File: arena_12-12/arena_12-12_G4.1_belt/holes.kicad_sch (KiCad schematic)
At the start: 4 parts

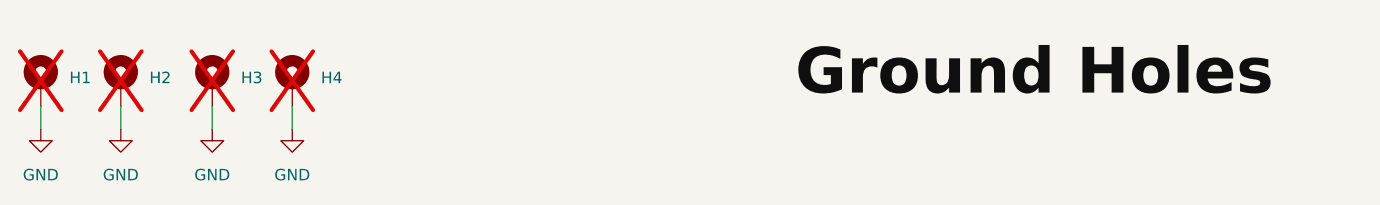
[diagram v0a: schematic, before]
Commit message: cleanup, belt with SMD power connector
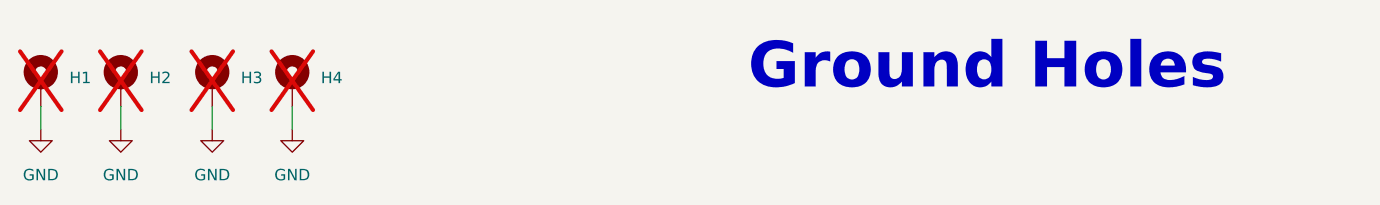
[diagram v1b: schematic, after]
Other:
- note added: "Ground Holes"
- title: 12-12 Teensy G4.1 Arena Belt Modular LED Display -> Arena 12-12 G4.1 Belt :: Modular LED Display
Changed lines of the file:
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@@
 	(paper "A4")
 	(title_block
-		(title "12-12 Teensy G4.1 Arena Belt Modular LED Display")
-		(date "2025-07-22")
-		(rev "v0.5.1")
+		(title "Arena 12-12 G4.1 Belt :: Modular LED Display")
+		(date "2025-07-24")
+		(rev "v0.1")
 		(company "MCN-NET @ Janelia")
+	)
+	(text "Ground Holes"
+		(exclude_from_sim no)
+		(at 147.066 28.702 0)
+		(effects
+			(font
+				(face "KiCad Font")
+				(size 5.08 5.08)
+				(thickness 1.016)
+				(bold yes)
+			)
+		)
 	)
 	(wire
@@
 		)
 	)
-	(label "Ground Holes"
-		(at 125.73 33.02 0)
-		(effects
-			(font
-				(size 5.08 5.08)
-				(thickness 1.016)
-				(bold yes)
-			)
-			(justify left bottom)
-		)
-	)
